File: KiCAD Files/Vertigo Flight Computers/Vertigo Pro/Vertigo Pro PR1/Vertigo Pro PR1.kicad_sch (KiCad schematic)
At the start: 148 parts, among them IC1 ICM-20602, IC2 DPS310XTSA1, J1 ST-LINK Conn, J2 USB_C_Receptacle_USB2.0, J3 FFC2A32-24-T, J4 Screw_Terminal, J5 Screw_Terminal, J6 Screw_Terminal, J7 Screw_Terminal, Q1 IRF530SPBF, Q2 MMBT3904-TP, Q3 MMBT3904-TP, Q4 IRF530SPBF, Q5 SI7149ADP-T1-GE3, Q6 MMBT3904-TP, Q7 MMBT3904-TP, Q8 IRF530SPBF, Q9 IRF530SPBF, SW1 SW_SPDT, U1 STM32F103C8Tx, U10 TPS79133DBVR, U11 TLV709, U12 TLV709, U13 TLV75528PDBV, U2 AP63203WU, U3 ESP32-S3-WROOM-1, U4 TLV75515PDBV, U6 W25Q64FV, U7 TPS2121RUXR, U8 NEO-6M-GPS, U9 24AA32A-I_MS, Y1 16MHz

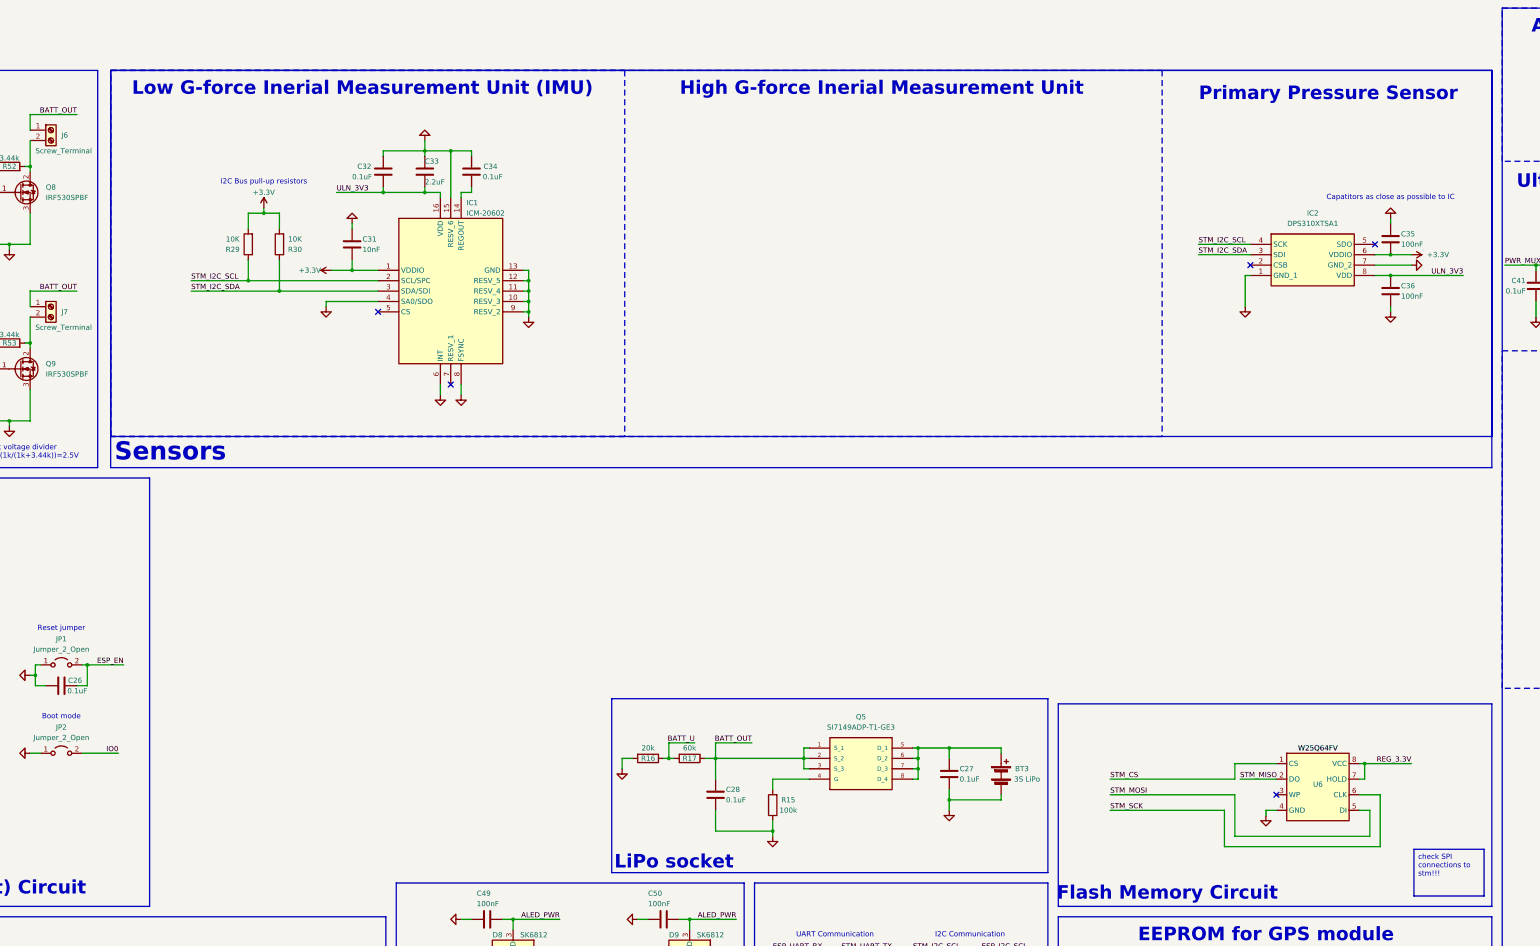
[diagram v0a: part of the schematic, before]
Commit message: High G-force IMU added, Low G-force IMU fix, added more annotations
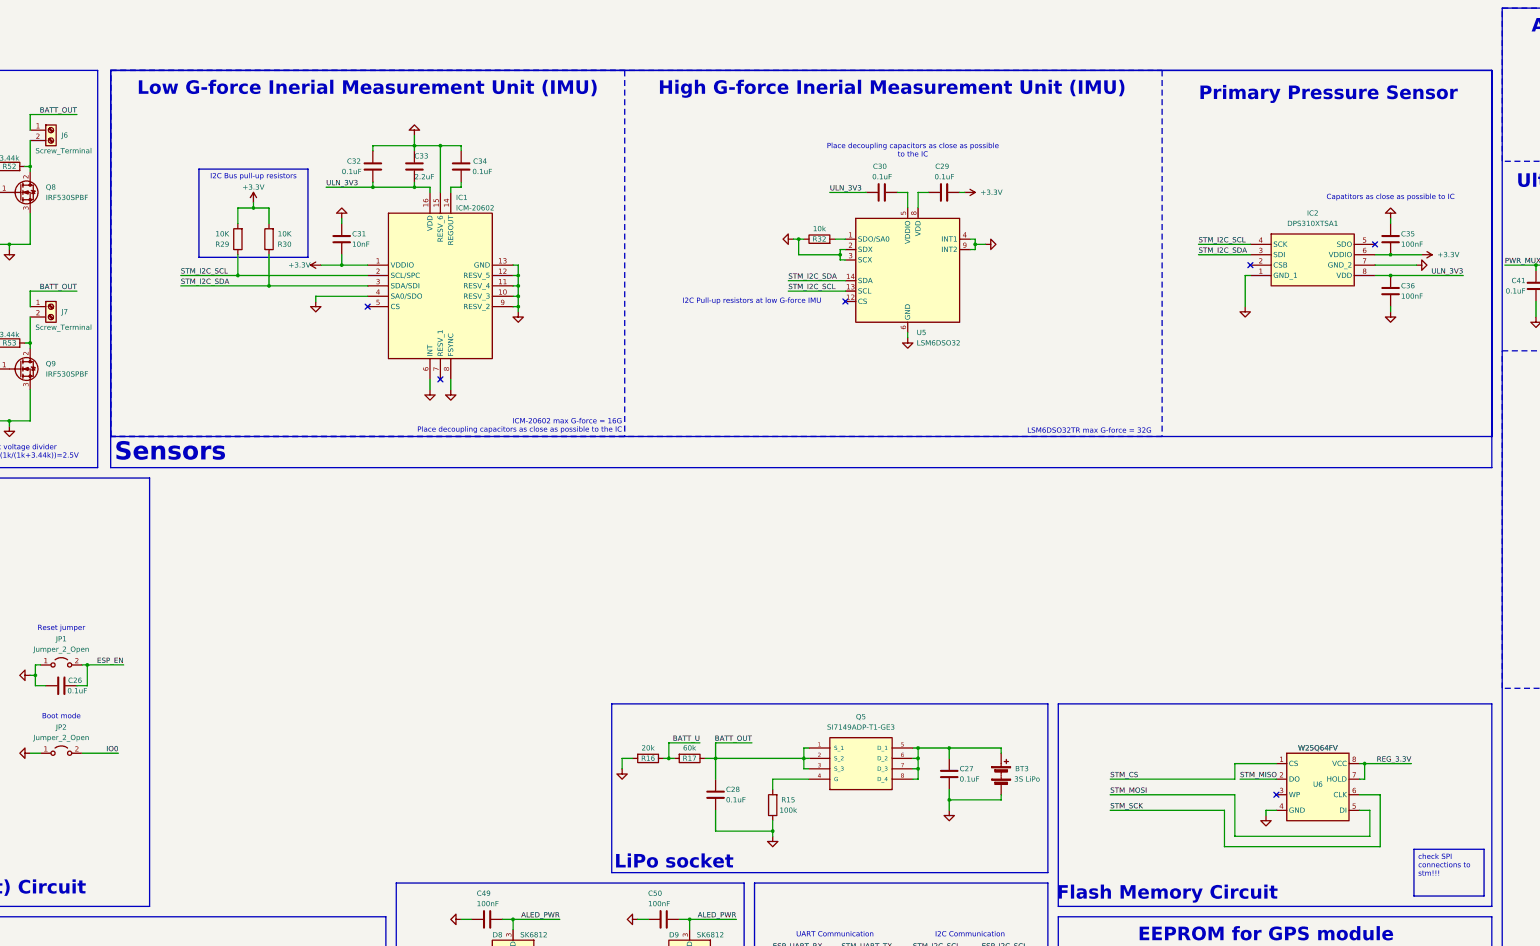
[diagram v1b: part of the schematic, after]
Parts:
- added C29, C30: 0.1uF, Capacitor_SMD:C_0402_1005Metric_Pad0.74x0.62mm_HandSolder, symbol Device:C
- added R32: 10k, Resistor_SMD:R_1206_3216Metric, symbol Device:R
- added U5: LSM6DSO32, Package_LGA:LGA-14_3x2.5mm_P0.5mm_LayoutBorder3x4y, symbol Sensor_Motion:LSM6DS3
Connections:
- net +3.3V: now also C29.2
- net AGND: now also R32.1, U5.2 (SDX), U5.3 (SCX), U5.4 (INT1), U5.6 (GND), U5.7 (GND), U5.9 (INT2)
- net DVP_VSYNC: now also U5.14 (SDA)
- net ESP_I2C_SCL: now also U5.13 (SCL)
- net ULN_3V3: now also C30.1
- new net: R32.2, U5.1 (SDO/SA0)
- new net: C29.1, U5.8 (VDD)
- new net: C30.2, U5.5 (VDDIO)
- no-connect marks 24 -> 25
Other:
- note added: "High G-force Inerial Measurement Unit (IMU)"
- note added: "I2C Pull-up resistors at low G-force IMU"
- note added: "ICM-20602 max G-force = 16G Place decoupling capacitors as close as possible to the IC"
- note added: "LSM6DSO32TR max G-force = 32G"
- note added: "Place decoupling capacitors as close as possible to the IC"
- note removed: "High G-force Inerial Measurement Unit"
- moved on the sheet: C31, C32, C33, C34, IC1, R29, R30

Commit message: Removed flash IC
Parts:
- removed U6: W25Q64FV, Vertigo Pro KiCad Libraries:SON127P600X500X80-9N, symbol Vertigo KiCad libraries:w25q64fv
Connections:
- net SPI_MISO renamed STM_SPI_MISO
- net SPI_MOSI renamed STM_SPI_MOSI
- net SPI_NSS renamed STM_SPI_NSS
- net SPI_SCK renamed STM_SPI_SCK
- no-connect marks 25 -> 24
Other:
- note removed: "Flash Memory Circuit"
- moved on the sheet: BT3, C27, C28, Q5, R15, R16, R17

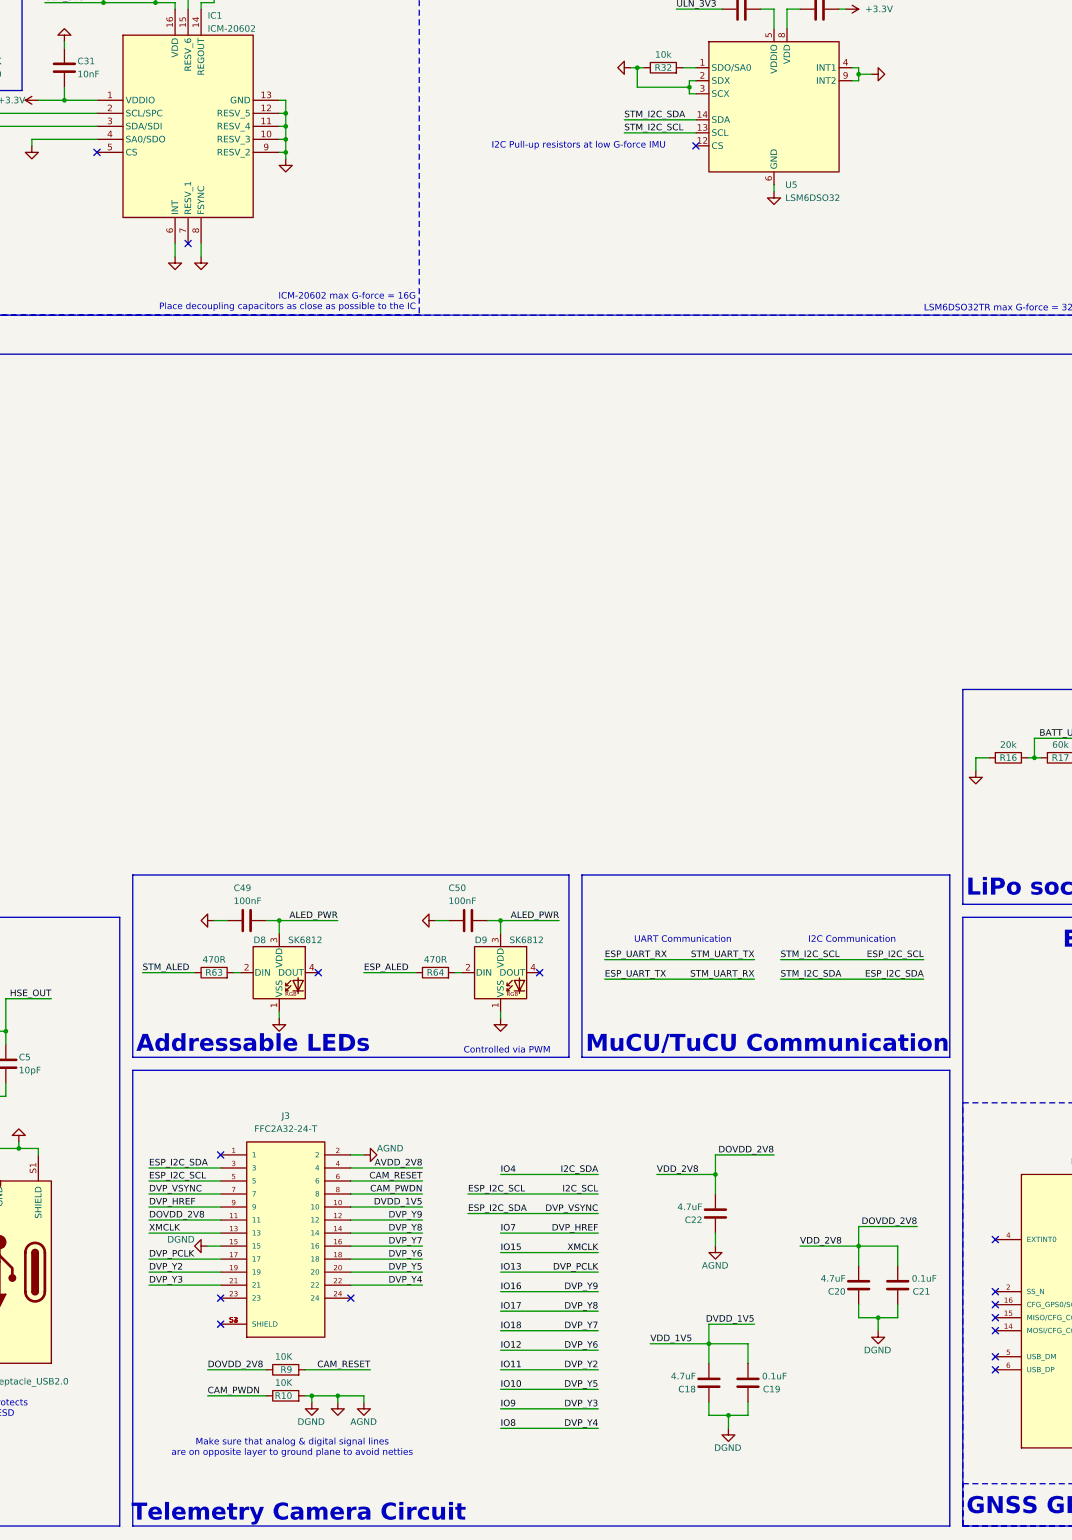
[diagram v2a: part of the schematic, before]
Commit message: High-G IMU fix
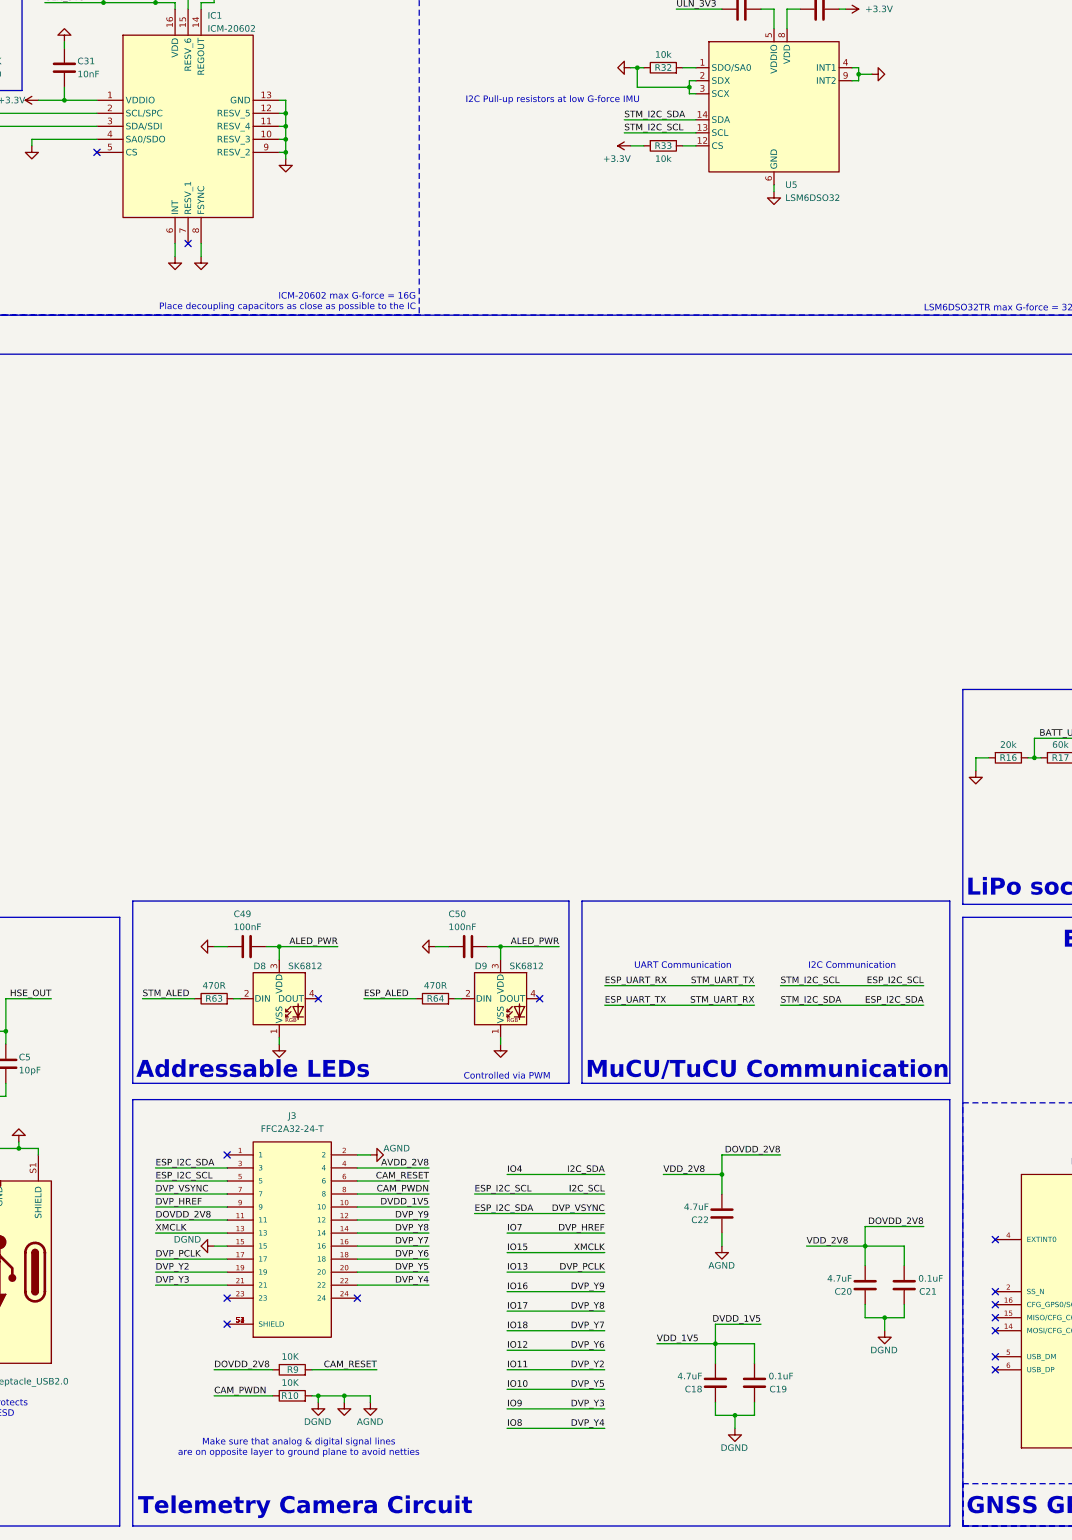
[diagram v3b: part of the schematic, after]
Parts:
- added R33: 10k, Resistor_SMD:R_1206_3216Metric, symbol Device:R
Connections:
- net +3.3V: now also R33.2
- net at U5.12 (CS): now also R33.1
- no-connect marks 24 -> 23
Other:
- moved on the sheet: C18, C19, C20, C21, C22, C49, C50, D8, D9, J3, R10, R63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

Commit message: Fix
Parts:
- added R54: 10k, Resistor_SMD:R_1206_3216Metric, symbol Device:R
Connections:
- net +3.3V: now also C30.2, U5.5 (VDDIO); no longer C29.2
- net AGND: now also C29.1, C30.1, R54.2; no longer U5.4 (INT1)
- net ULN_3V3: now also C29.2, U5.8 (VDD); no longer C30.1
- new net: R54.1, U5.4 (INT1)
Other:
- moved on the sheet: C29, C30, R32, R33, U5

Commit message: fix
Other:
- note added: "For GNSS IC & USB D+ pull-up"
- note added: "Pressure Sensor"
- note added: "Ultralow Noise 3.3V Voltage Regulator"
- note removed: "Primary Pressure Sensor"
- note removed: "Ultralow Noise 3.3V Voltage Regulator for GNSS & USB D+ pull-up"
- moved on the sheet: C35, C36, IC2, R3

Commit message: Sch fix
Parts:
- removed C29, C30: 0.1uF, Capacitor_SMD:C_0402_1005Metric_Pad0.74x0.62mm_HandSolder, symbol Device:C
- removed C39: 1uF, Capacitor_SMD:C_0603_1608Metric_Pad1.08x0.95mm_HandSolder, symbol Device:C
- removed R32, R33, R54: 10k, Resistor_SMD:R_1206_3216Metric, symbol Device:R
- removed R35, R37, R39, R41: 5k, Resistor_SMD:R_0603_1608Metric, symbol Device:R
- removed R36: 64.4k, Resistor_SMD:R_0603_1608Metric, symbol Device:R
- removed R38: 23.7k, Resistor_SMD:R_0603_1608Metric, symbol Device:R
- removed R40: 10.2k, Resistor_SMD:R_0603_1608Metric, symbol Device:R
- removed R42: 21.5k, Resistor_SMD:R_0603_1608Metric, symbol Device:R
- removed U5: LSM6DSO32, Package_LGA:LGA-14_3x2.5mm_P0.5mm_LayoutBorder3x4y, symbol Sensor_Motion:LSM6DS3
- removed U7: TPS2121RUXR, Vertigo Pro KiCad Libraries:RUX0012A, symbol 2024-05-25_13-45-03:TPS2121RUXR
- added D3: D_Schottky, symbol Device:D_Schottky
- J2: value USB_C_Receptacle_USB2.0 -> USB_C_2.0
- R34: value 18.2k -> 480R
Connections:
- net 5V_USB_RAW: now also D3.1 (K); no longer D5.1 (K), J2.A4 (VBUS), J2.A9 (VBUS), J2.B4 (VBUS), J2.B9 (VBUS)
- net AGND: now also R34.1; no longer C28.2, R15.1
- net BATT_OUT: no longer R34.2
- new net USB_VBUS_D_CUTOFF: C28.2, D3.2 (A), D5.1 (K), J2.A4 (VBUS), J2.A9 (VBUS), J2.B4 (VBUS), J2.B9 (VBUS), R15.1, R34.2
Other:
- note added: "Protection agains diode failure"
- note removed: "High G-force Inerial Measurement Unit (IMU)"
- note removed: "I2C Pull-up resistors at low G-force IMU"
- note removed: "LSM6DSO32TR max G-force = 32G"
- note removed: "Place decoupling capacitors as close as possible to the IC"
- note removed: "Power MUX"
- note removed: "Vcp2 = 5V(5k/(5k+10.2k)) = 1.64V"
- note removed: "Vpr1 = 12V(5k/(5k+18.2k)) = 2.59V"
- moved on the sheet: BT3, C23, C24, C27, C28, C31, C32, C33, C34, C35, C36, C41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

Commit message: LiPo/USB protection fix
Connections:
- net BATT_OUT is gone; now on net VCC: C28.1, J4.1 (Pin_1), J5.1 (Pin_1), J6.1 (Pin_1), J7.1 (Pin_1), Q5.1 (S_1), Q5.2 (S_2), Q5.3 (S_3), R17.1
- net PWR_MUX is gone; now on net VCC: C12.1, C41.2, C47.2, U11.1 (IN), U12.1 (IN), U2.2 (EN), U2.3 (IN)
- net 5V_USB_RAW renamed VCC
